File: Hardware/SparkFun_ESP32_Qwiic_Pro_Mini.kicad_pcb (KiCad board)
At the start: 2 copper layers, 33 x 17.8 mm, 80 parts, among them J1 Conn_01x06, J2 Conn_01x12, J3 Conn_01x12, J5 Qwiic_Vertical, SW1 Reset, SW2 Boot, U1 ESP32-PICO-V3-02, U2 AP2112K-3.3

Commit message: Remove stray label
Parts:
- removed kibuzzard-6501F573: G***, kibuzzard-6501F573
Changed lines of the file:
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@@
     (attr board_only exclude_from_pos_files exclude_from_bom)
     (fp_text reference "kibuzzard-6501F591" (at 0 3.521075) (layer "B.SilkS") hide
-        (effects (font (size 0 0)) (justify mirror))
+        (effects (font (size 0 0) (thickness 0.15)) (justify mirror))
     )
     (fp_text value "G***" (at 0 -3.521075) (layer "B.SilkS") hide
-        (effects (font (size 0 0)) (justify mirror))
+        (effects (font (size 0 0) (thickness 0.15)) (justify mirror))
     )
     (fp_poly
@@
       )
       (stroke (width 0) (type solid)) (fill solid) (layer "B.SilkS"))
-  )
-  (footprint "kibuzzard-6501F573" (layer "B.Cu")
-    (at 170.434 124.206 180)
-    (descr "Generated with KiBuzzard")
-    (tags "kb_params=eyJBbGlnbm1lbnRDaG9pY2UiOiAiQ2VudGVyIiwgIkNhcExlZnRDaG9pY2UiOiAiWyIsICJDYXBSaWdodENob2ljZSI6ICIpIiwgIkZvbnRDb21ib0JveCI6ICJGcmVkb2thT25lIiwgIkhlaWdodEN0cmwiOiAiMC44IiwgIkxheWVyQ29tYm9Cb3giOiAiRi5TaWxrUyIsICJNdWx0aUxpbmVUZXh0IjogIlBXUiIsICJQYWRkaW5nQm90dG9tQ3RybCI6ICIzIiwgIlBhZGRpbmdMZWZ0Q3RybCI6ICIzIiwgIlBhZGRpbmdSaWdodEN0cmwiOiAiMyIsICJQYWRkaW5nVG9wQ3RybCI6ICIzIiwgIldpZHRoQ3RybCI6ICIifQ==")
-    (attr board_only exclude_from_pos_files exclude_from_bom)
-    (fp_text reference "kibuzzard-6501F573" (at 0 3.679825) (layer "B.SilkS") hide
-        (effects (font (size 0 0)) (justify mirror))
-    )
-    (fp_text value "G***" (at 0 -3.679825) (layer "B.SilkS") hide
-        (effects (font (size 0 0)) (justify mirror))
-    )
-    (fp_poly
-      (pts
-        (xy -1.333818 0.240665)
-        (xy -1.492568 0.240665)
-        (xy -1.492568 0.015875)
-        (xy -1.332548 0.015875)
-        (xy -1.257618 0.043815)
-        (xy -1.220788 0.127635)
-        (xy -1.257618 0.21209)
-        (xy -1.333818 0.240665)
-      )
-      (stroke (width 0) (type solid)) (fill solid) (layer "B.SilkS"))
-    (fp_poly
-      (pts
-        (xy 0.578802 0.015875)
-        (xy 0.741362 0.015875)
-        (xy 0.815023 0.043815)
-        (xy 0.851853 0.127635)
-        (xy 0.815023 0.21209)
-        (xy 0.738822 0.240665)
-        (xy 0.578802 0.240665)
-        (xy 0.578802 0.015875)
-      )
-      (stroke (width 0) (type solid)) (fill solid) (layer "B.SilkS"))
-    (fp_poly
-      (pts
-        (xy -1.717358 0.631825)
-        (xy -1.876108 0.631825)
-        (xy -1.876108 -0.631825)
-        (xy -1.717358 -0.631825)
-        (xy -1.605598 -0.631825)
-        (xy -1.605598 -0.464185)
-        (xy -1.676083 -0.452437)
-        (xy -1.709738 -0.417195)
-        (xy -1.717358 -0.351155)
-        (xy -1.717358 0.353695)
-        (xy -1.715453 0.39751)
-        (xy -1.703388 0.431165)
-        (xy -1.669733 0.456882)
-        (xy -1.604328 0.465455)
-        (xy -1.332548 0.465455)
-        (xy -1.258746 0.456424)
-        (xy -1.186356 0.429331)
-        (xy -1.115378 0.384175)
-        (xy -1.06807 0.33782)
-        (xy -1.030288 0.277495)
-        (xy -1.005523 0.206375)
-        (xy -0.997268 0.127635)
-        (xy -1.005523 0.049054)
-        (xy -1.030288 -0.02159)
-        (xy -1.06807 -0.081439)
-        (xy -1.115378 -0.127635)
-        (xy -1.186498 -0.172791)
-        (xy -1.259311 -0.199884)
-        (xy -1.333818 -0.208915)
-        (xy -1.492568 -0.208915)
-        (xy -1.492568 -0.352425)
-        (xy -1.494473 -0.39624)
-        (xy -1.506538 -0.429895)
-        (xy -1.540193 -0.455613)
-        (xy -1.605598 -0.464185)
-        (xy -1.605598 -0.631825)
-        (xy -0.082233 -0.631825)
-        (xy -0.082233 -0.464185)
-        (xy -0.147002 -0.44323)
-        (xy -0.183197 -0.401955)
-        (xy -0.331787 0.036195)
-        (xy -0.382638 -0.114071)
-        (xy -0.422415 -0.231623)
-        (xy -0.451117 -0.316459)
-        (xy -0.468744 -0.368579)
-        (xy -0.475298 -0.387985)
-        (xy -0.486728 -0.409575)
-        (xy -0.507048 -0.434975)
-        (xy -0.576898 -0.464185)
-        (xy -0.643573 -0.445135)
-        (xy -0.678498 -0.407035)
-        (xy -0.687388 -0.387985)
-        (xy -0.932498 0.316865)
-        (xy -0.946468 0.379095)
-        (xy -0.925195 0.424498)
-        (xy -0.861377 0.459105)
-        (xy -0.794703 0.471805)
-        (xy -0.748983 0.451485)
-        (xy -0.720408 0.389255)
-        (xy -0.580708 -0.034925)
-        (xy -0.442278 0.382905)
-        (xy -0.417195 0.42799)
-        (xy -0.377508 0.456565)
-        (xy -0.324802 0.465455)
-        (xy -0.264477 0.4445)
-        (xy -0.228918 0.403225)
-        (xy -0.082868 -0.037465)
-        (xy 0.056832 0.389255)
-        (xy 0.073343 0.432435)
-        (xy 0.096837 0.45974)
-        (xy 0.139383 0.473075)
-        (xy 0.199073 0.460375)
-        (xy 0.26289 0.424815)
-        (xy 0.284162 0.379095)
-        (xy 0.268923 0.316865)
-        (xy 0.025082 -0.387985)
-        (xy 0.016192 -0.409575)
-        (xy -0.017462 -0.44323)
-        (xy -0.082233 -0.464185)
-        (xy -0.082233 -0.631825)
-        (xy 0.941387 -0.631825)
-        (xy 0.941387 -0.473075)
-        (xy 0.900747 -0.46101)
-        (xy 0.877252 -0.436245)
-        (xy 0.860601 -0.399979)
-        (xy 0.827581 -0.323356)
-        (xy 0.778192 -0.206375)
-        (xy 0.738822 -0.208915)
-        (xy 0.578802 -0.208915)
-        (xy 0.578802 -0.352425)
-        (xy 0.576897 -0.39624)
-        (xy 0.564833 -0.429895)
-        (xy 0.531177 -0.455613)
-        (xy 0.465773 -0.464185)
-        (xy 0.395287 -0.452437)
-        (xy 0.361632 -0.417195)
-        (xy 0.354012 -0.351155)
-        (xy 0.354012 0.353695)
-        (xy 0.355917 0.39751)
-        (xy 0.367982 0.431165)
-        (xy 0.401637 0.456882)
-        (xy 0.467042 0.465455)
-        (xy 0.741362 0.465455)
-        (xy 0.815164 0.456424)
-        (xy 0.887554 0.429331)
-        (xy 0.958532 0.384175)
-        (xy 1.004887 0.33782)
-        (xy 1.042352 0.277495)
-        (xy 1.067118 0.206375)
-        (xy 1.075372 0.127635)
-        (xy 1.064789 0.037606)
-        (xy 1.033039 -0.041134)
-        (xy 0.980122 -0.108585)
-        (xy 1.002136 -0.160655)
-        (xy 1.030922 -0.227118)
-        (xy 1.066482 -0.307975)
-        (xy 1.085532 -0.374015)
-        (xy 1.065847 -0.418465)
-        (xy 1.006792 -0.455295)
-        (xy 0.941387 -0.473075)
-        (xy 0.941387 -0.631825)
-        (xy 1.085532 -0.631825)
-        (xy 1.244282 -0.631825)
-        (xy 1.306212 -0.628783)
-        (xy 1.367545 -0.619685)
-        (xy 1.427692 -0.604619)
-        (xy 1.486071 -0.58373)
-        (xy 1.542123 -0.55722)
-        (xy 1.595306 -0.525343)
-        (xy 1.645108 -0.488407)
-        (xy 1.69105 -0.446768)
-        (xy 1.73269 -0.400826)
-        (xy 1.769626 -0.351023)
-        (xy 1.801502 -0.29784)
-        (xy 1.828013 -0.241789)
-        (xy 1.848901 -0.183409)
-        (xy 1.863967 -0.123263)
-        (xy 1.873065 -0.06193)
-        (xy 1.876107 0)
-        (xy 1.873065 0.06193)
-        (xy 1.863967 0.123263)
-        (xy 1.848901 0.183409)
-        (xy 1.828013 0.241789)
-        (xy 1.801502 0.29784)
-        (xy 1.769626 0.351023)
-        (xy 1.73269 0.400826)
-        (xy 1.69105 0.446768)
-        (xy 1.645108 0.488407)
-        (xy 1.595306 0.525343)
-        (xy 1.542123 0.55722)
-        (xy 1.486071 0.58373)
-        (xy 1.427692 0.604619)
-        (xy 1.367545 0.619685)
-        (xy 1.306212 0.628783)
-        (xy 1.244282 0.631825)
-        (xy 1.085532 0.631825)
-        (xy -1.717358 0.631825)
-      )
-      (stroke (width 0) (type solid)) (fill solid) (layer "B.SilkS"))

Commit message: Post review changes.
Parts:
- JP1: value ~ -> PWR
- moved C3 1.65 mm to (151.1, 118.6), turned to 180 degrees
- moved C6 1.65 mm to (151.1, 120.3)
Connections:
- C3 pad 1: +3.3V -> ~{RESET}
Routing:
- net ~{RESET}: track 40.7 -> 42.3 mm
- net +3.3V: track 63.3 -> 61.6 mm
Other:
- board text added: "Material: TG135-140"

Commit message: Post design review fixes.
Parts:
- added Ref**: Val**, SparkFun-Aesthetic:OSHW_Logo_2.5mm, B.Cu at (131.6, 124.2)
- U3: footprint SparkFun-Aesthetic:Ordering_Instructions -> SparkFun-Aesthetic:ORDERING_INSTRUCTIONS
- moved U3 1.27 mm to (185.5, 81.4)

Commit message: Add fiducials
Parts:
- added FID1: Fiducial_0.5, SparkFun-Aesthetic:Fiducial_0.5mm_Mask1mm, F.Cu at (132.3, 118.7)
- added FID2: Fiducial_0.5, SparkFun-Aesthetic:Fiducial_0.5mm_Mask1mm, F.Cu at (159.8, 126.2)

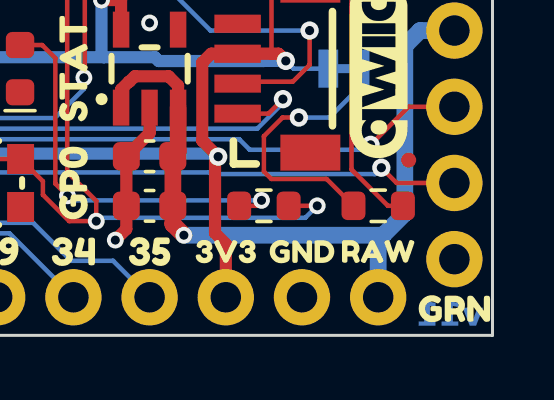
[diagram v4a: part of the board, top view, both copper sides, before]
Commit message: Fix bad silk. Update to v12.
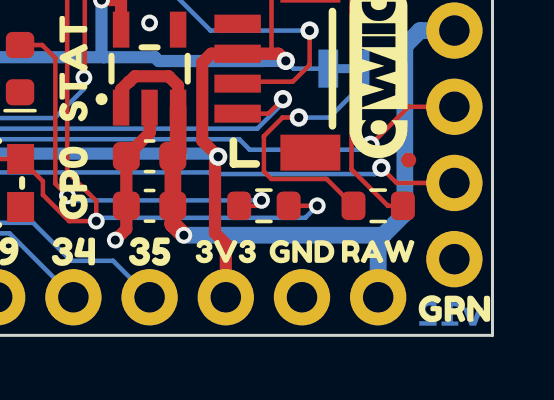
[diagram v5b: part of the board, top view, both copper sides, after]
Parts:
- removed kibuzzard-64DED6C8: G***, kibuzzard-64DED6C8
- added kibuzzard-653C16CF: G***, kibuzzard-653C16CF, B.Cu at (135.9, 129.3)
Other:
- board text added: "v12"
- board text removed: "v11"

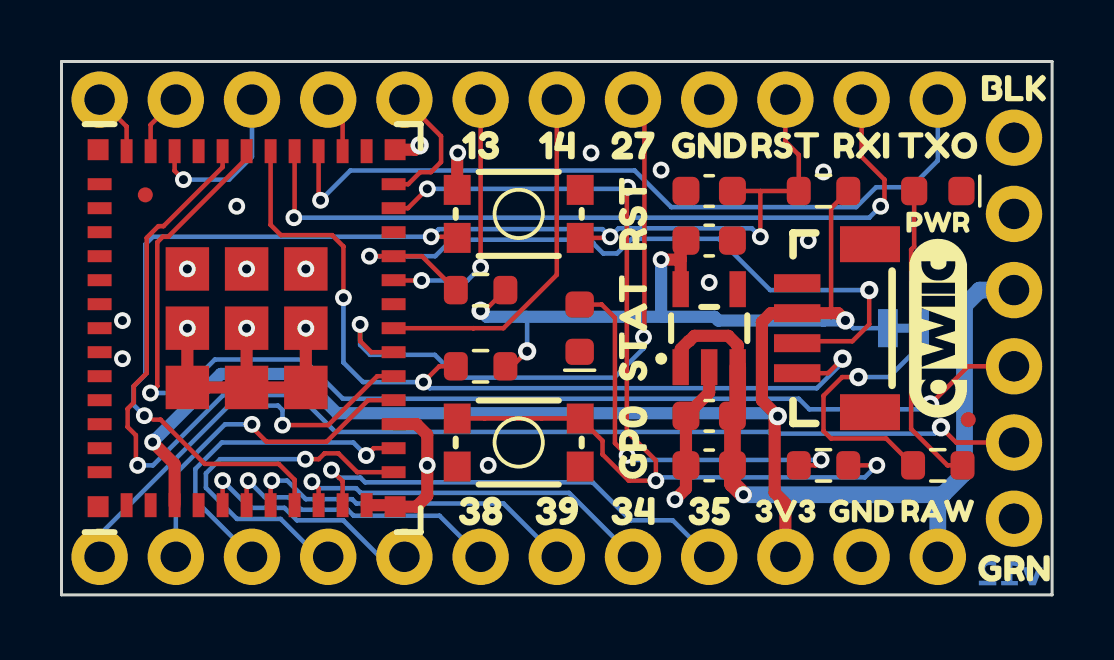
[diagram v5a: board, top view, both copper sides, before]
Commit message: Update 3D models
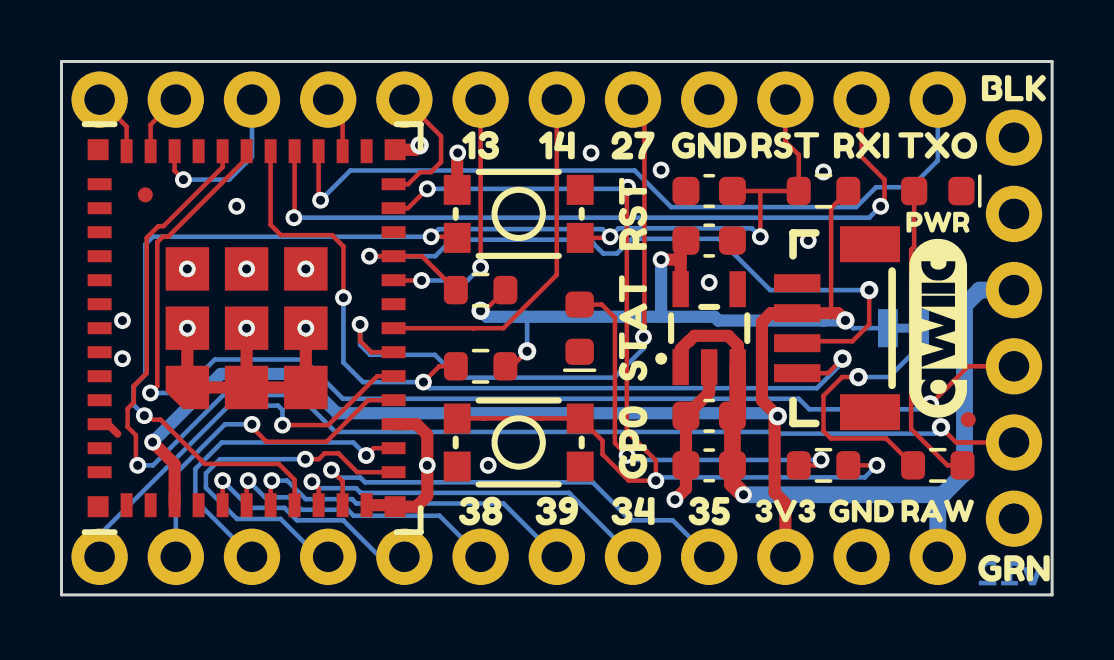
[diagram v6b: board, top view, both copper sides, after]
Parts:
- D1: footprint SparkFun-LED:LED_0603_1608Metric -> SparkFun-LED:LED_0603_1608Metric_Green
- D2: footprint SparkFun-LED:LED_0603_1608Metric -> SparkFun-LED:LED_0603_1608Metric_Red
- J1: footprint SparkFun-Connector:1X06 -> SparkFun-Connector:1x06
- J2, J3: footprint SparkFun-Connector:1X12 -> SparkFun-Connector:1x12
- J5: footprint SparkFun-Connector:JST04_1MM_Vertical -> SparkFun-Connector:JST_SMD_1.0mm-4_Vertical
- JP1: footprint SparkFun-Jumper:SMT-JUMPER_2_NC_TRACE_SILK -> SparkFun-Jumper:Jumper_2_NC_Trace
- SW1, SW2: footprint SparkFun-Switch:Momentary_SMD_4.6x2.8mm -> SparkFun-Switch:Push_SMD_4.6x2.8mm_h2.5mm
- U1: footprint SparkFun-RF:ESP32-MINI -> SparkFun-RF:ESP32-PICO-MINI
- U3: footprint SparkFun-Aesthetic:ORDERING_INSTRUCTIONS -> SparkFun-Aesthetic:Ordering_Instructions
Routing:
- net GND: track 22.4 -> 23.1 mm
